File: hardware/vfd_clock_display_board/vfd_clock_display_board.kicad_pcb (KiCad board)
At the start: 2 copper layers, 124.9 x 94.6 mm, 112 parts, among them J1 Conn_01x12_Pin, Q1 MMDT5551, Q10 2N3906, Q11 2N3906, Q12 2N3906, Q13 MMDT5551, Q14 MMDT5551, Q15 2N3906, Q16 2N3906, Q17 2N3906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

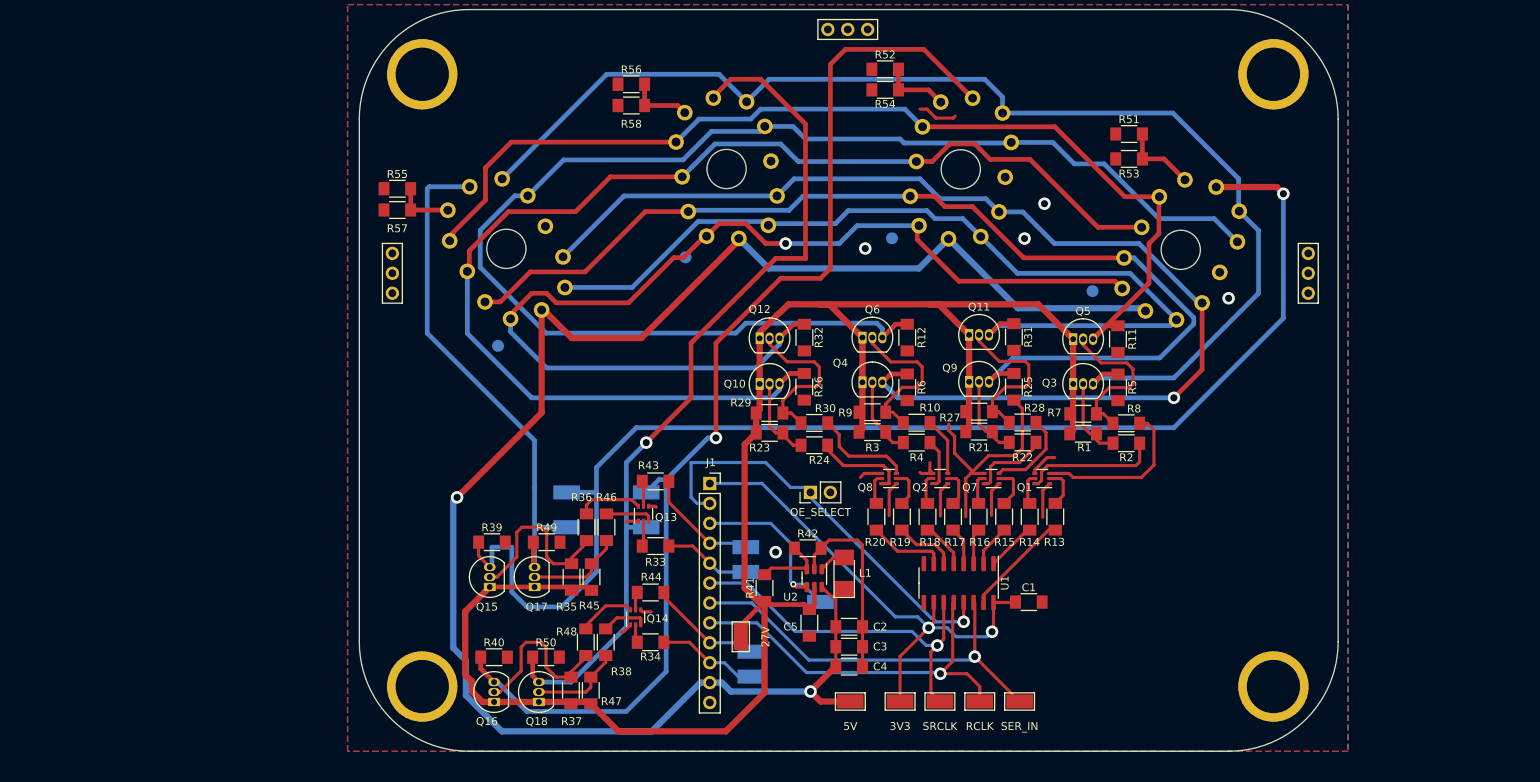
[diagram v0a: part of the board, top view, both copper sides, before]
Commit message: Somekind of hardware change, fix spi transaction
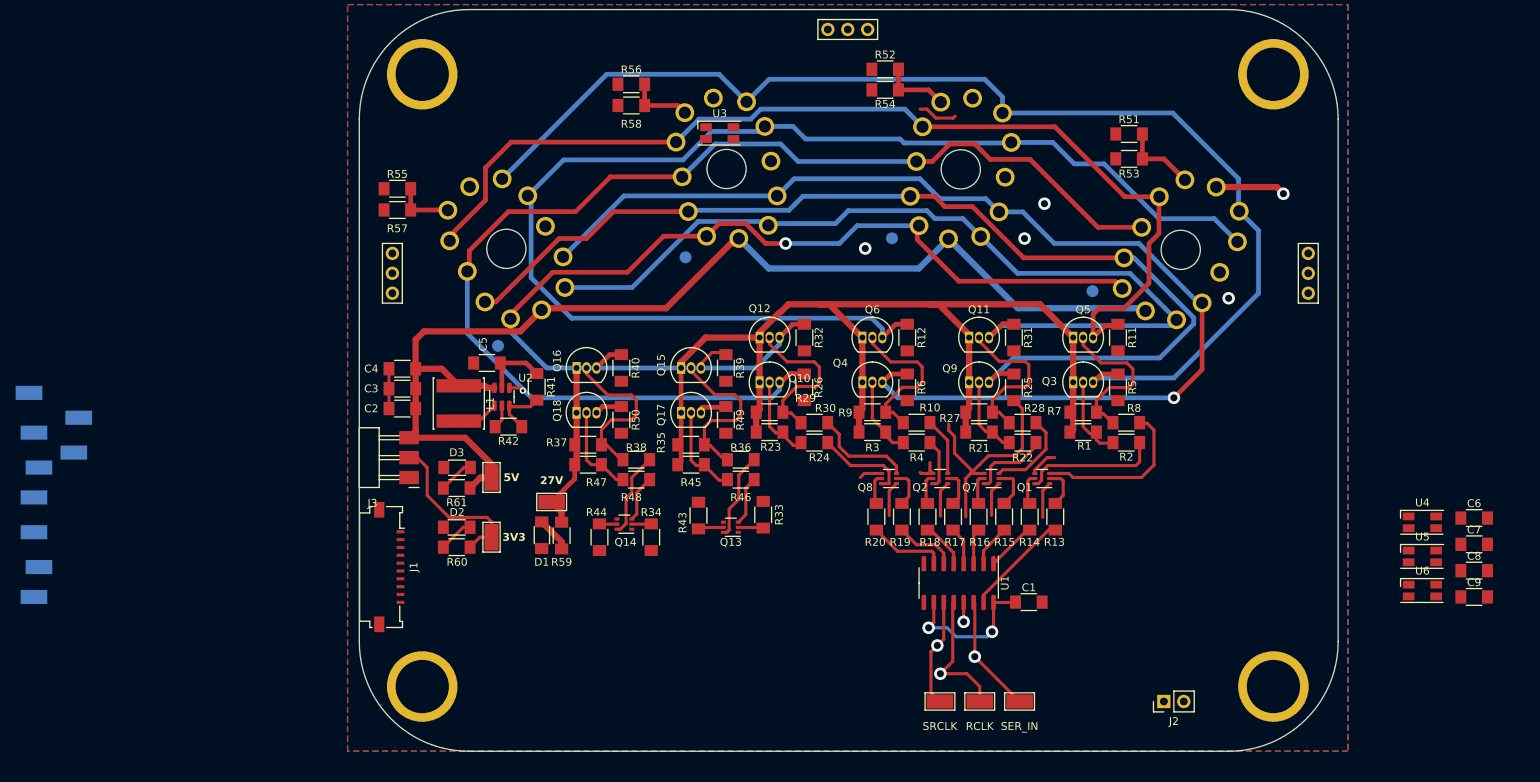
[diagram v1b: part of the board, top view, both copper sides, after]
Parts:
- added C6: 1uF, Fab:C_1206, F.Cu at (232.6, 120.1)
- added C7: 1uF, Fab:C_1206, F.Cu at (232.6, 123.5)
- added C8: 1uF, Fab:C_1206, F.Cu at (232.6, 126.8)
- added C9: 1uF, Fab:C_1206, F.Cu at (232.6, 130.2)
- added D1: LED_1206, fab:LED_1206, F.Cu at (113.7, 122.3)
- added D2: LED_1206, fab:LED_1206, F.Cu at (102.8, 121.3)
- added D3: LED_1206, fab:LED_1206, F.Cu at (102.9, 113.7)
- added J3: Conn_PinHeader_1x03_P2.54mm_Horizontal_SMD, fab:PinHeader_1x03_P2.54mm_Horizontal_SMD, F.Cu at (96.7, 114.9)
- added R59: 5.1K, Fab:R_1206, F.Cu at (116.2, 122.3)
- added R60: 5.1K, Fab:R_1206, F.Cu at (102.8, 123.8)
- added R61: 5.1K, Fab:R_1206, F.Cu at (102.8, 116.3)
- added U3: LED_ADDR_Worldsemi_WS2812B, Fab:LED_RGB_CreeLED_CLV1A-FKB, F.Cu at (136.4, 71.0)
- added U4: LED_ADDR_Worldsemi_WS2812B, Fab:LED_RGB_CreeLED_CLV1A-FKB, F.Cu at (226.0, 120.7)
- added U5: LED_ADDR_Worldsemi_WS2812B, Fab:LED_RGB_CreeLED_CLV1A-FKB, F.Cu at (226.0, 125.0)
- added U6: LED_ADDR_Worldsemi_WS2812B, Fab:LED_RGB_CreeLED_CLV1A-FKB, F.Cu at (226.0, 129.4)
- J1: value Conn_01x12_Pin -> Conn_01x10_MountingPin; footprint Connector_PinSocket_2.54mm:PinSocket_1x12_P2.54mm_Vertical -> Connector_FFC-FPC:Molex_200528-0100_1x10-1MP_P1.00mm_Horizontal
- L1: footprint Fab:L_1210 -> Inductor_SMD:L_Changjiang_FNR6045S
- VFD1, VFD2, VFD3, VFD4: footprint VFD:IV-22 -> VFD:IV-22 - Pin
- moved TLV_EN 97.1 mm to (54.0, 111.8)
- moved VFD1_EN 93.5 mm to (48.3, 104.1)
- moved VFD1_EN 92.0 mm to (48.9, 130.2)
- moved VFD1_EN 91.4 mm to (49.5, 126.4)
- moved VFD0_EN 87.3 mm to (54.6, 107.3)
- moved VFD2_GRID 78.5 mm to (48.9, 109.2)
- moved VFD3_GRID 78.1 mm to (48.9, 121.9)
- moved C4 68.5 mm to (95.9, 101.1), turned to 180 degrees
- moved VFD1_GRID 68.1 mm to (48.9, 117.5)
- moved VFD0_GRID 67.4 mm to (49.5, 113.7)
- moved C3 65.8 mm to (95.9, 103.6), turned to 180 degrees
- moved C2 63.4 mm to (95.9, 106.1), turned to 180 degrees
- moved 3V3 56.2 mm to (107.3, 122.6), turned to -90 degrees
- moved 5V 54.0 mm to (107.3, 114.9), turned to -90 degrees
- moved L1 53.7 mm to (103.1, 105.5), turned to -90 degrees
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- renumbered OE_SELECT to J2
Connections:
- J1 pad 1: PWR_3V3 -> /OE
- J1 pad 10: /VFD2_EN -> /LED_DIN
- J1 pad 2: /OE -> /TLV_EN
- J1 pad 3: /TLV_EN -> /VFD1_EN
- J1 pad 4: /VFD1_EN -> /VFD0_EN
- J1 pad 5: /VFD0_EN -> /SRCLK
- J1 pad 6: /SRCLK -> /SER_IN
- J1 pad 7: /SER_IN -> /RCLK
- J1 pad 8: /RCLK -> /VFD3_EN
- J1 pad 9: /VFD3_EN -> /VFD2_EN
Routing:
- net /VFD0_GRID: track 165.5 -> 12.7 mm
- net /VFD2_GRID: track 143.9 -> 3.88 mm, vias 1 -> 0
- net /VFD3_GRID: track 111.2 -> 3.50 mm, vias 1 -> 0
- net PWR_5V: track 217.0 -> 146.3 mm, vias 2 -> 0
- net 27V: track 226.7 -> 162.6 mm
- net /VFD1_GRID: track 66.8 -> 3.24 mm
- net /OE: track 53.6 -> 2.47 mm
- net /SER_IN: track 52.1 -> 15.1 mm
- net /SRCLK: track 46.1 -> 13.8 mm
- net /RCLK: track 48.9 -> 16.8 mm
- net PWR_3V3: track 65.4 -> 40.2 mm
- net PWR_GND: track 92.8 -> 70.8 mm, vias 5 -> 4
- net /TLV_EN: track 23.0 -> 1.87 mm
- net /VFD1_EN: track 14.9 -> 0.00 mm
- net /VFD3_EN: track 14.5 -> 0.00 mm
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
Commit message: I forgor
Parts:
- removed REF** (x3): PinHeader_1x03, Fab:PinHeader_1x03_P2.54mm_Vertical_THT_D1mm
- added OE: TestPoint_Keystone_5015_Micro-Minature, TestPoint:TestPoint_Keystone_5015_Micro-Minature, F.Cu at (160.0, 137.8)
- TLV_EN, VFD0_EN, VFD0_GRID, VFD1_EN, VFD1_GRID, VFD2_GRID, VFD3_GRID: moved to F.Cu
- VFD2_EN, VFD3_EN: renamed from VFD1_EN; moved to F.Cu
- moved VFD0_GRID 163.4 mm to (207.6, 72.4), turned to 0 degrees
- moved VFD2_GRID 132.9 mm to (172.7, 61.0), turned to 0 degrees
- moved C6 125.6 mm to (114.9, 76.2), turned to 90 degrees
- moved VFD3_GRID 107.3 mm to (135.9, 59.1), turned to 0 degrees
- moved U4 102.7 mm to (136.3, 70.7), turned to -170 degrees
- moved C7 101.2 mm to (148.0, 67.9), turned to 90 degrees
- moved VFD1_EN 80.7 mm to (119.4, 142.2)
- moved U5 79.7 mm to (168.0, 70.3), turned to 170 degrees
- moved VFD0_EN 78.7 mm to (125.1, 142.2), turned to 0 degrees
- moved VFD1_GRID 78.3 mm to (108.0, 66.0), turned to 0 degrees
- moved C8 75.9 mm to (180.3, 71.8), turned to 90 degrees
- moved TLV_EN 68.1 mm to (118.7, 132.7), turned to 0 degrees
- moved VFD2_EN 65.9 mm to (113.7, 142.2), turned to 0 degrees
- moved VFD3_EN 60.5 mm to (108.0, 142.2), turned to 0 degrees
- moved U6 55.6 mm to (198.1, 81.3), turned to 150 degrees
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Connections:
- C6 pad 2: Net-(U3-VDD) -> PWR_GND
- C7 pad 2: Net-(U4-VDD) -> PWR_GND
- C8 pad 2: Net-(U5-VDD) -> PWR_GND
- C9 pad 2: Net-(U6-VDD) -> PWR_GND
- J1 pad 1: /OE -> /LED_DIN
- J1 pad 10: /LED_DIN -> /SER_IN
- J1 pad 3: /VFD1_EN -> /VFD3_EN
- J1 pad 4: /VFD0_EN -> /VFD2_EN
- J1 pad 5: /SRCLK -> /VFD1_EN
- J1 pad 6: /SER_IN -> /VFD0_EN
- J1 pad 7: /RCLK -> /SRCLK
- J1 pad 8: /VFD3_EN -> /RCLK
- J1 pad 9: /VFD2_EN -> /OE
- U3 pad 1: Net-(U3-VDD) -> PWR_5V
- U4 pad 1: Net-(U4-VDD) -> PWR_5V
- U5 pad 1: Net-(U5-VDD) -> PWR_5V
- U6 pad 1: Net-(U6-VDD) -> PWR_5V
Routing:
- net PWR_5V: track 146.3 -> 293.2 mm, vias 0 -> 4
- net /VFD2_GRID: track 3.88 -> 148.9 mm
- net PWR_GND: track 70.8 -> 187.9 mm, vias 4 -> 9
- net /VFD0_GRID: track 12.7 -> 115.4 mm
- net /VFD3_GRID: track 3.50 -> 98.6 mm
- net /LED_DIN: track 0.00 -> 78.1 mm, vias 0 -> 2
- net /VFD1_GRID: track 3.24 -> 73.2 mm
- net PWR_3V3: track 40.2 -> 105.1 mm, vias 2 -> 3
- net /TLV_EN: track 1.87 -> 54.8 mm, vias 1 -> 2
- net /VFD3_EN: track 0.00 -> 48.1 mm
- net /VFD2_EN: track 0.00 -> 37.5 mm
- net /OE: track 2.47 -> 39.0 mm, vias 1 -> 0
- net /RCLK: track 16.8 -> 51.1 mm, vias 1 -> 0
- net /SRCLK: track 13.8 -> 46.9 mm, vias 1 -> 0
- net Net-(U5-DOUT): track 0.00 -> 31.5 mm
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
